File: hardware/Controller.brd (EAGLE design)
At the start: 38.1 x 58.4 mm, 70 parts, among them Q1 MOSFET-NCHANNEL2N7002PW, Q2 BSS84PW, Q3 BSS84PW, U3 MMA8652FC, U4 MCP6002MS, U5 TXS0101DCK, U6 LCD_1.8, U7 VREG

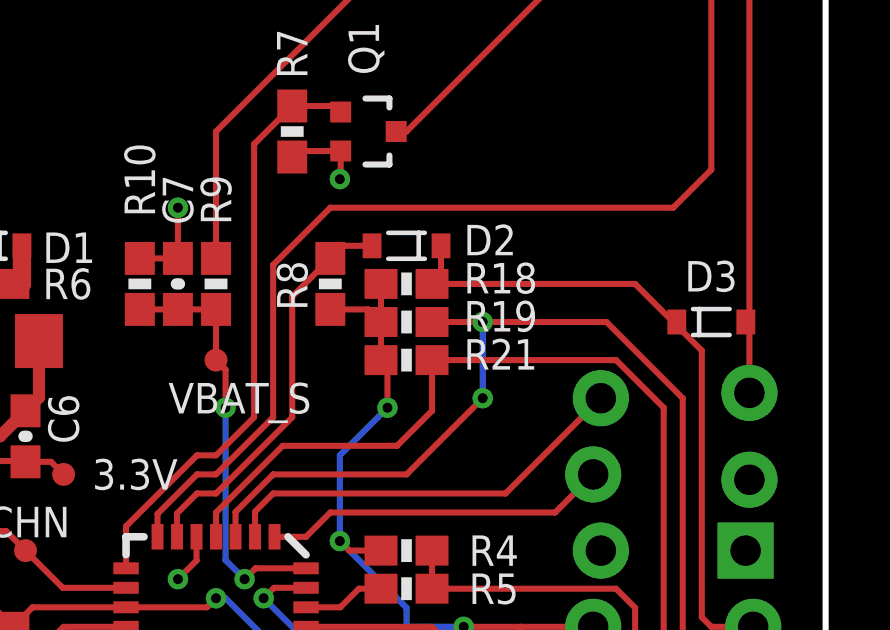
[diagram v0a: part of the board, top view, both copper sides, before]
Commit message: hardware: Remove R18
It was wrong to pull to 3.3V behind the diode, resulting in always enabling the VREG
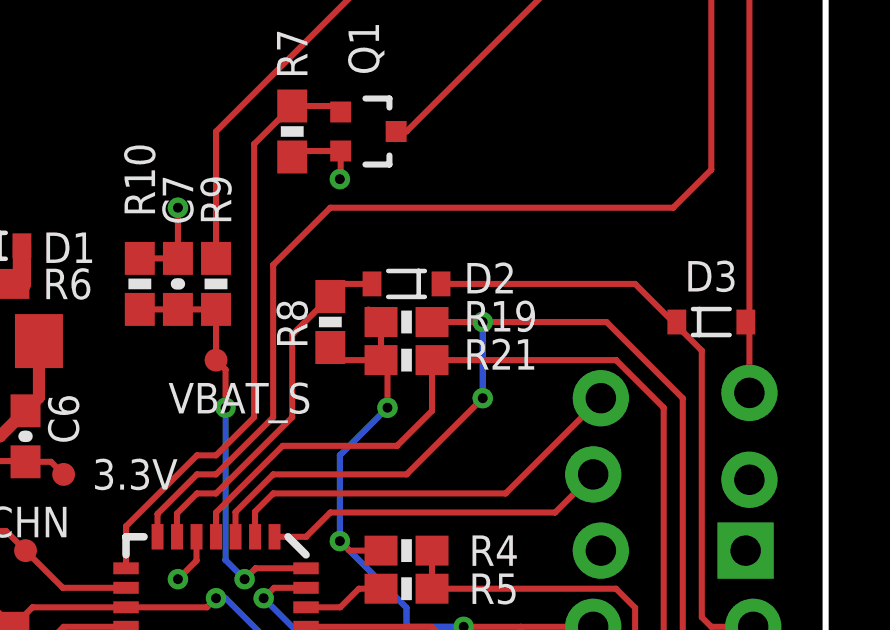
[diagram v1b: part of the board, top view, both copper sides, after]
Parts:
- removed R18: 10k, SparkFun-Resistors:0603-RES
- moved D2 1.27 mm to (24.1, 34.3)
- moved R8 1.27 mm to (21.6, 33.0)
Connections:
- net !KNOB_PUSH: no longer R18.2
- net 3.3V: no longer R18.1
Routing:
- net !KNOB_PUSH: track 22.3 -> 20.6 mm
- net !KNOB_PUSH_SENSE: track 13.3 -> 12.1 mm
- net 3.3V: track 72.9 -> 72.2 mm
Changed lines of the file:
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@@
 <attribute name="VALUE" x="35.306" y="4.953" size="1.016" layer="27" font="vector" ratio="14" rot="R180"/>
-</element>
-<element name="R18" library="SparkFun-Resistors" package="0603-RES" value="10k" x="24.13" y="34.29" smashed="yes">
-<attribute name="NAME" x="26.035" y="33.9725" size="1.016" layer="25" font="vector" ratio="14"/>
 </element>
 <element name="R19" library="SparkFun-Resistors" package="0603-RES" value="10k" x="24.13" y="33.02" smashed="yes">
@@
 <attribute name="VALUE" x="33.274" y="31.623" size="1.016" layer="27" ratio="14"/>
 </element>
-<element name="R8" library="SparkFun-Resistors" package="0603-RES" value="100k" x="21.59" y="34.29" smashed="yes" rot="R90">
-<attribute name="NAME" x="20.828" y="33.401" size="1.016" layer="25" font="vector" ratio="14" rot="R90"/>
-<attribute name="VALUE" x="22.733" y="33.274" size="1.016" layer="27" font="vector" ratio="14" rot="R90"/>
-</element>
-<element name="D2" library="Parts" package="SOD-323" value="1N4148WS" x="24.13" y="35.56" smashed="yes" rot="R180">
-<attribute name="NAME" x="26.035" y="35.2425" size="1.016" layer="25" ratio="14"/>
-<attribute name="VALUE" x="25.146" y="36.957" size="1.016" layer="27" ratio="14" rot="R180"/>
+<element name="R8" library="SparkFun-Resistors" package="0603-RES" value="100k" x="21.59" y="33.02" smashed="yes" rot="R90">
+<attribute name="NAME" x="20.828" y="32.131" size="1.016" layer="25" font="vector" ratio="14" rot="R90"/>
+<attribute name="VALUE" x="22.733" y="32.004" size="1.016" layer="27" font="vector" ratio="14" rot="R90"/>
+</element>
+<element name="D2" library="Parts" package="SOD-323" value="1N4148WS" x="24.13" y="34.29" smashed="yes" rot="R180">
+<attribute name="NAME" x="26.035" y="33.9725" size="1.016" layer="25" ratio="14"/>
+<attribute name="VALUE" x="25.146" y="35.687" size="1.016" layer="27" ratio="14" rot="R180"/>
 </element>
 <element name="U6" library="Parts" package="LCD_1.8" value="LCD_1.8" x="19.05" y="0" smashed="yes"/>
@@
 <contactref element="U2" pad="5"/>
 <contactref element="3.3V" pad="P$1"/>
-<contactref element="R18" pad="1"/>
 <contactref element="R19" pad="1"/>
 <contactref element="R21" pad="1"/>
@@
 <wire x1="4.66" y1="15.24" x2="5.5" y2="14.4" width="0.2032" layer="1"/>
 <wire x1="5.5" y1="14.4" x2="5.5" y2="13.97" width="0.2032" layer="1"/>
-<wire x1="23.28" y1="34.29" x2="23.28" y2="33.02" width="0.2032" layer="1"/>
 <wire x1="23.28" y1="33.02" x2="23.28" y2="31.75" width="0.2032" layer="1"/>
-<wire x1="21.59" y1="33.44" x2="22.86" y2="33.44" width="0.2032" layer="1"/>
 <wire x1="22.86" y1="33.44" x2="23.28" y2="33.02" width="0.2032" layer="1"/>
 <wire x1="11.01" y1="22.86" x2="11.66" y2="23.51" width="0.2032" layer="1"/>
@@
 <wire x1="26.035" y1="22.86" x2="24.13" y2="22.86" width="0.2032" layer="16"/>
 <wire x1="27.94" y1="21.17" x2="27.94" y2="22.86" width="0.2032" layer="1"/>
+<wire x1="21.59" y1="32.17" x2="22.01" y2="31.75" width="0.2032" layer="1"/>
+<wire x1="22.01" y1="31.75" x2="23.28" y2="31.75" width="0.2032" layer="1"/>
 </signal>
 <signal name="GND">
@@
 <signal name="!KNOB_PUSH">
 <contactref element="KNOB" pad="2"/>
-<contactref element="R18" pad="2"/>
 <contactref element="D3" pad="C"/>
 <contactref element="D2" pad="C"/>
 <wire x1="33.9725" y1="23.1775" x2="33.9725" y2="32.0675" width="0.2032" layer="1"/>
-<wire x1="31.75" y1="34.29" x2="24.98" y2="34.29" width="0.2032" layer="1"/>
-<wire x1="25.28" y1="35.56" x2="25.28" y2="34.59" width="0.2032" layer="1"/>
-<wire x1="25.28" y1="34.59" x2="24.98" y2="34.29" width="0.2032" layer="1"/>
 <wire x1="33.9725" y1="23.1775" x2="34.29" y2="22.86" width="0.2032" layer="1"/>
 <wire x1="34.29" y1="22.86" x2="35.687" y2="22.86" width="0.2032" layer="1"/>
@@
 <wire x1="33.02" y1="33.02" x2="31.75" y2="34.29" width="0.2032" layer="1"/>
 <wire x1="33.14" y1="33.02" x2="33.02" y2="33.02" width="0.2032" layer="1"/>
+<wire x1="25.28" y1="34.29" x2="31.75" y2="34.29" width="0.2032" layer="1"/>
 </signal>
 <signal name="N$34">
@@
 <contactref element="R8" pad="2"/>
 <contactref element="U1" pad="6"/>
-<wire x1="22.98" y1="35.56" x2="22.01" y2="35.56" width="0.2032" layer="1"/>
-<wire x1="22.01" y1="35.56" x2="21.59" y2="35.14" width="0.2032" layer="1"/>
 <wire x1="16.48" y1="25.86" x2="16.48" y2="26.64" width="0.2032" layer="1"/>
 <wire x1="16.48" y1="26.64" x2="17.145" y2="27.305" width="0.2032" layer="1"/>
 <wire x1="17.145" y1="27.305" x2="17.78" y2="27.305" width="0.2032" layer="1"/>
 <wire x1="17.78" y1="27.305" x2="20.32" y2="29.845" width="0.2032" layer="1"/>
-<wire x1="20.32" y1="29.845" x2="20.32" y2="33.87" width="0.2032" layer="1"/>
-<wire x1="20.32" y1="33.87" x2="21.59" y2="35.14" width="0.2032" layer="1"/>
+<wire x1="20.32" y1="29.845" x2="20.32" y2="32.6" width="0.2032" layer="1"/>
+<wire x1="20.32" y1="32.6" x2="21.59" y2="33.87" width="0.2032" layer="1"/>
+<wire x1="21.59" y1="33.87" x2="22.01" y2="34.29" width="0.2032" layer="1"/>
+<wire x1="22.01" y1="34.29" x2="22.98" y2="34.29" width="0.2032" layer="1"/>
 </signal>
 <signal name="!TFT_RST">

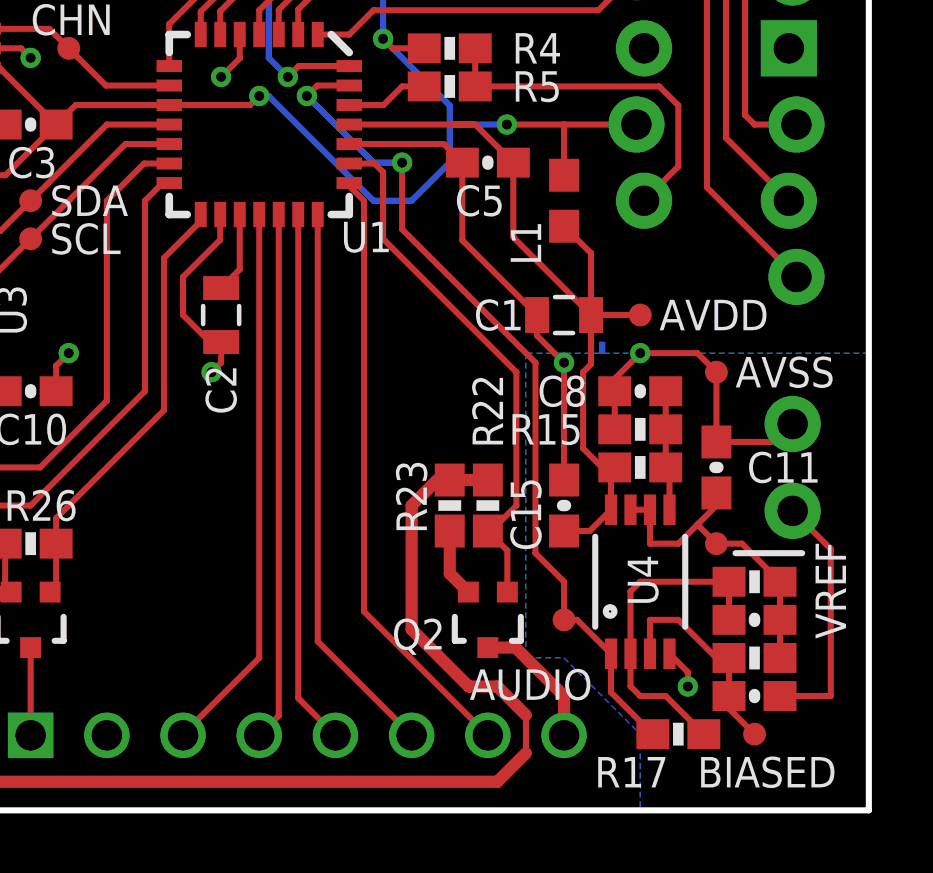
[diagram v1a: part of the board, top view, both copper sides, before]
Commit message: hardware: Route TFT SPI pins to RPx pins
Previously, the MCU pins used for TFT SPI could not be driven by a SPI peripheral.
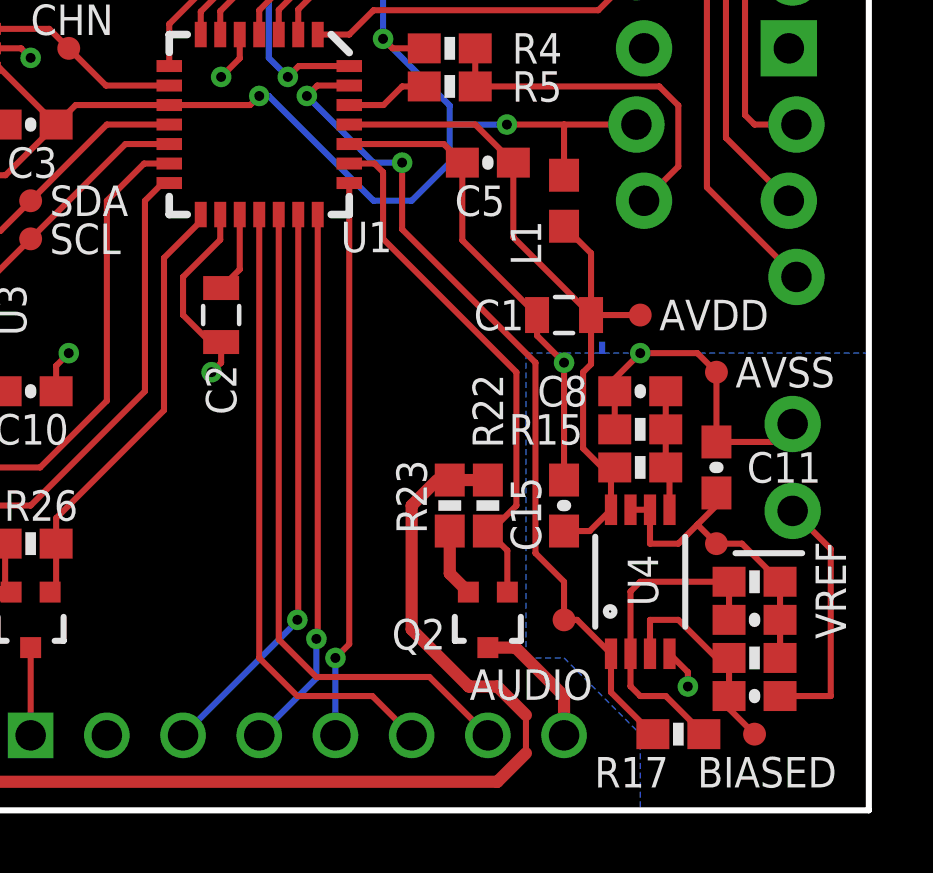
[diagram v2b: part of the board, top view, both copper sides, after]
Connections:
- net !TFT_CS: now also U1.20; no longer U1.18
- net !TFT_RST: now also U1.21; no longer U1.19
- net TFT_A0\: now also U1.22; no longer U1.20
- net TFT_SCK: now also U1.19; no longer U1.22
- net TFT_SDA: now also U1.18; no longer U1.21
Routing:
- net TFT_SDA: track 18.7 -> 20.9 mm
- net TFT_SCK: track 20.3 -> 22.5 mm
- net VREF: track 11.0 -> 12.3 mm
- net TFT_A0\: track 17.9 -> 18.6 mm, vias 0 -> 1
- net !TFT_CS: track 18.4 -> 19.0 mm, vias 0 -> 1
- net !TFT_RST: track 17.6 -> 18.2 mm, vias 0 -> 1
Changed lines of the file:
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@@
 <layer number="23" name="tOrigins" color="15" fill="1" visible="yes" active="yes"/>
 <layer number="24" name="bOrigins" color="15" fill="1" visible="yes" active="yes"/>
-<layer number="25" name="tNames" color="7" fill="1" visible="yes" active="yes"/>
-<layer number="26" name="bNames" color="7" fill="1" visible="yes" active="yes"/>
+<layer number="25" name="tNames" color="7" fill="1" visible="no" active="yes"/>
+<layer number="26" name="bNames" color="7" fill="1" visible="no" active="yes"/>
 <layer number="27" name="tValues" color="7" fill="1" visible="no" active="yes"/>
 <layer number="28" name="bValues" color="7" fill="1" visible="no" active="yes"/>
@@
 <layer number="50" name="dxf" color="7" fill="1" visible="no" active="no"/>
 <layer number="51" name="tDocu" color="6" fill="1" visible="yes" active="yes"/>
-<layer number="52" name="bDocu" color="7" fill="1" visible="yes" active="yes"/>
+<layer number="52" name="bDocu" color="7" fill="1" visible="no" active="yes"/>
 <layer number="53" name="tGND_GNDA" color="7" fill="9" visible="no" active="no"/>
 <layer number="54" name="bGND_GNDA" color="1" fill="9" visible="no" active="no"/>
@@
 <wire x1="32.385" y1="9.525" x2="33.02" y2="10.16" width="0.2032" layer="1"/>
 <wire x1="33.02" y1="10.16" x2="33.02" y2="10.58" width="0.2032" layer="1"/>
-<wire x1="35.14" y1="7.62" x2="35.14" y2="5.08" width="0.2032" layer="1"/>
 <wire x1="35.14" y1="7.62" x2="33.87" y2="8.89" width="0.2032" layer="1"/>
 <wire x1="33.87" y1="8.89" x2="33.02" y2="8.89" width="0.2032" layer="1"/>
 <wire x1="33.02" y1="8.89" x2="32.385" y2="9.525" width="0.2032" layer="1"/>
 <contactref element="C12" pad="1"/>
-<wire x1="35.14" y1="5.08" x2="35.14" y2="6.35" width="0" layer="19" extent="1-1"/>
+<wire x1="35.14" y1="5.08" x2="35.14" y2="6.35" width="0.2032" layer="1"/>
+<wire x1="35.14" y1="5.08" x2="35.14" y2="7.62" width="0.2032" layer="1"/>
 </signal>
 <signal name="N$3">
@@
 <signal name="!TFT_RST">
 <contactref element="U6" pad="!RESET"/>
-<contactref element="U1" pad="19"/>
-<wire x1="17.78" y1="2.5" x2="18.43" y2="3.15" width="0.2032" layer="1"/>
-<wire x1="18.43" y1="3.15" x2="18.43" y2="19.86" width="0.2032" layer="1"/>
+<contactref element="U1" pad="21"/>
+<wire x1="17.78" y1="2.5" x2="19.685" y2="4.405" width="0.2032" layer="16"/>
+<wire x1="19.685" y1="4.405" x2="19.685" y2="5.715" width="0.2032" layer="16"/>
+<via x="19.685" y="5.715" extent="1-16" drill="0.3302"/>
+<wire x1="19.685" y1="5.715" x2="19.73" y2="5.76" width="0.2032" layer="1"/>
+<wire x1="19.73" y1="5.76" x2="19.73" y2="19.86" width="0.2032" layer="1"/>
 </signal>
 <signal name="TFT_A0\">
 <contactref element="U6" pad="A0"/>
-<contactref element="U1" pad="20"/>
-<wire x1="20.32" y1="2.5" x2="19.08" y2="3.74" width="0.2032" layer="1"/>
-<wire x1="19.08" y1="3.74" x2="19.08" y2="19.86" width="0.2032" layer="1"/>
+<contactref element="U1" pad="22"/>
+<via x="20.32" y="5.08" extent="1-16" drill="0.3302"/>
+<wire x1="20.32" y1="5.08" x2="20.32" y2="2.5" width="0.2032" layer="16"/>
+<wire x1="20.32" y1="5.08" x2="20.78" y2="5.54" width="0.2032" layer="1"/>
+<wire x1="20.78" y1="5.54" x2="20.78" y2="20.91" width="0.2032" layer="1"/>
 </signal>
 <signal name="TFT_SDA">
 <contactref element="U6" pad="SDA"/>
-<contactref element="U1" pad="21"/>
-<wire x1="22.86" y1="2.5" x2="19.73" y2="5.63" width="0.2032" layer="1"/>
-<wire x1="19.73" y1="5.63" x2="19.73" y2="19.86" width="0.2032" layer="1"/>
+<contactref element="U1" pad="18"/>
+<wire x1="17.78" y1="5.08" x2="17.78" y2="19.86" width="0.2032" layer="1"/>
+<wire x1="17.78" y1="5.08" x2="19.05" y2="3.81" width="0.2032" layer="1"/>
+<wire x1="19.05" y1="3.81" x2="21.55" y2="3.81" width="0.2032" layer="1"/>
+<wire x1="21.55" y1="3.81" x2="22.86" y2="2.5" width="0.2032" layer="1"/>
 </signal>
 <signal name="TFT_SCK">
 <contactref element="U6" pad="SCK"/>
-<contactref element="U1" pad="22"/>
-<wire x1="21.2725" y1="6.6275" x2="21.2725" y2="20.32" width="0.2032" layer="1"/>
-<wire x1="21.2725" y1="20.32" x2="20.78" y2="20.8125" width="0.2032" layer="1"/>
-<wire x1="20.78" y1="20.8125" x2="20.78" y2="20.91" width="0.2032" layer="1"/>
-<wire x1="25.4" y1="2.5" x2="21.2725" y2="6.6275" width="0.2032" layer="1"/>
+<contactref element="U1" pad="19"/>
+<wire x1="18.43" y1="19.86" x2="18.43" y2="5.7" width="0.2032" layer="1"/>
+<wire x1="18.43" y1="5.7" x2="19.685" y2="4.445" width="0.2032" layer="1"/>
+<wire x1="19.685" y1="4.445" x2="23.455" y2="4.445" width="0.2032" layer="1"/>
+<wire x1="23.455" y1="4.445" x2="25.4" y2="2.5" width="0.2032" layer="1"/>
 </signal>
 <signal name="N$12">
@@
 <signal name="!TFT_CS">
 <contactref element="U6" pad="!CS"/>
-<contactref element="U1" pad="18"/>
-<wire x1="15.24" y1="2.5" x2="15.24" y2="2.54" width="0.2032" layer="1"/>
-<wire x1="15.24" y1="2.54" x2="17.78" y2="5.08" width="0.2032" layer="1"/>
-<wire x1="17.78" y1="5.08" x2="17.78" y2="19.86" width="0.2032" layer="1"/>
+<contactref element="U1" pad="20"/>
+<wire x1="19.08" y1="19.86" x2="19.08" y2="6.38" width="0.2032" layer="1"/>
+<wire x1="19.08" y1="6.38" x2="19.05" y2="6.35" width="0.2032" layer="1"/>
+<via x="19.05" y="6.35" extent="1-16" drill="0.3302"/>
+<wire x1="19.05" y1="6.35" x2="19.05" y2="6.31" width="0.2032" layer="16"/>
+<wire x1="19.05" y1="6.31" x2="15.24" y2="2.5" width="0.2032" layer="16"/>
 </signal>
 <signal name="N$13">
